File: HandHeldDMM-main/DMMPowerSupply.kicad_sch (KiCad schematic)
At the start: 30 parts, among them J8 Conn_01x01, J9 Conn_01x01, U12 XC62KN33302PR-G, U2 LM358, U8 AMS1117-3.3

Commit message: More pcb work
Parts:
- R24: footprint Resistor_SMD:R_0402_1005Metric_Pad0.72x0.64mm_HandSolder -> Resistor_SMD:R_0603_1608Metric_Pad0.98x0.95mm_HandSolder; LCSC Price 0.05 -> 0.09; Store https://www.lcsc.com/product-detail/Chip-Resistor-Surface-Mount_FOJAN-FRC0402P000-TS_C2906877.html -> https://www.lcsc.com/product-detail/Chip-Resistor-Surface-Mount_FOJAN-FRC0603P000-TS_C2907080.html
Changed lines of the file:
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@@
       (effects (font (size 1.27 1.27)))
     )
-    (property "Footprint" "Resistor_SMD:R_0402_1005Metric_Pad0.72x0.64mm_HandSolder" (at 74.295 60.198 90)
+    (property "Footprint" "Resistor_SMD:R_0603_1608Metric_Pad0.98x0.95mm_HandSolder" (at 74.295 60.198 90)
       (effects (font (size 1.27 1.27)) hide)
     )
-    (property "Datasheet" "https://datasheet.lcsc.com/lcsc/2308241947_FOJAN-FRC0402P000-TS_C2906877.pdf" (at 74.295 58.42 0)
+    (property "Datasheet" "https://datasheet.lcsc.com/lcsc/2308241947_FOJAN-FRC0603P000-TS_C2907080.pdf" (at 74.295 58.42 0)
       (effects (font (size 1.27 1.27)) hide)
     )
-    (property "LCSC Price" "0.05" (at 74.295 58.42 0)
+    (property "LCSC Price" "0.09" (at 74.295 58.42 0)
       (effects (font (size 1.27 1.27)) hide)
     )
@@
       (effects (font (size 1.27 1.27)) hide)
     )
-    (property "Store" "https://www.lcsc.com/product-detail/Chip-Resistor-Surface-Mount_FOJAN-FRC0402P000-TS_C2906877.html" (at 74.295 58.42 0)
+    (property "Store" "https://www.lcsc.com/product-detail/Chip-Resistor-Surface-Mount_FOJAN-FRC0603P000-TS_C2907080.html" (at 74.295 58.42 0)
       (effects (font (size 1.27 1.27)) hide)
     )

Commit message: PCB rev 1 with schematic change ideas
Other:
- note added: "Voltage doubler - Larger input voltage for easier rail splitting - Larger opamp supply voltage helps reduce common mode noise"
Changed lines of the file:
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@@
+    (effects (font (size 1.27 1.27)) (justify left bottom))
+  )
+  (text "Voltage doubler\n- Larger input voltage for easier rail splitting\n- Larger opamp supply voltage helps reduce common mode noise"
+    (at 63.5 -1.27 0)
     (effects (font (size 1.27 1.27)) (justify left bottom))
   )

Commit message: Its going
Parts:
- removed C10 (x4): 1uF, Capacitor_SMD:C_0402_1005Metric_Pad0.74x0.62mm_HandSolder, symbol Device:C
- removed C15, C24: 10uF, Capacitor_SMD:C_0603_1608Metric_Pad1.08x0.95mm_HandSolder, symbol Device:C
- removed C17, C19, C21, C22: 100nF, Capacitor_SMD:C_0402_1005Metric_Pad0.74x0.62mm_HandSolder, symbol Device:C
- removed D1: LED, LED_SMD:LED_0603_1608Metric_Pad1.05x0.95mm_HandSolder, symbol Device:LED
- removed R1, R3: 100K, Resistor_SMD:R_0603_1608Metric_Pad0.98x0.95mm_HandSolder, symbol Device:R
- removed R12: 1k, Resistor_SMD:R_0603_1608Metric_Pad0.98x0.95mm_HandSolder, symbol Device:R
- removed R24: 0R, Resistor_SMD:R_0603_1608Metric_Pad0.98x0.95mm_HandSolder, symbol Device:R
- removed TP1, TP2, TP3, TP4: TestPoint, TestPoint:TestPoint_Pad_D2.0mm, symbol Connector:TestPoint
- removed U12: XC62KN33302PR-G, Package_TO_SOT_SMD:SOT-89-3, symbol Regulator_Linear:XC6206PxxxMR
- removed U2: LM358, Package_SO:SOP-8_3.9x4.9mm_P1.27mm, symbol Amplifier_Operational:LM358
- added C10 (x2): 1uF, Capacitor_SMD:C_0402_1005Metric_Pad0.74x0.62mm_HandSolder, symbol Device:C
- added C28, C36, C37, C39: 10uf, symbol Device:C_Polarized
- added C38, C40: C, symbol Device:C
- added C42, C43: 100nF, Capacitor_SMD:C_0402_1005Metric_Pad0.74x0.62mm_HandSolder, symbol Device:C
- added D4, D5: D, symbol Device:D
- added D6: LED, LED_SMD:LED_0603_1608Metric_Pad1.05x0.95mm_HandSolder, symbol Device:LED
- added R67: 1k, Resistor_SMD:R_0603_1608Metric_Pad0.98x0.95mm_HandSolder, symbol Device:R
- added U24: AMS1117-5.0, Package_TO_SOT_SMD:SOT-223-3_TabPin2, symbol Regulator_Linear:AMS1117-5.0
- added U26, U27, U28: TL7660CDR, Package_SO:SOIC-8_3.9x4.9mm_P1.27mm, symbol Regulator_SwitchedCapacitor:LMC7660
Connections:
- net BattOut- is gone; now on net GND: J9.1 (Pin_1)
- net GND: now also C10.2, C10.2, C37.1, C39.1, C40.1, C42.2, C43.2, R67.2, U24.1 (GND), U26.8 (V+), U27.3 (GND), U28.3 (GND), U28.5 (VOUT)
- net BattOut+ renamed +9V
- net +9V: now also C10.1, C42.1, U24.3 (VI), U27.8 (V+)
- new net: D4.2 (A), U28.8 (V+)
- new net: C28.1, U26.2 (CAP+)
- new net: C37.2, U26.3 (GND), U27.5 (VOUT)
- new net: C28.2, U26.4 (CAP-)
- new net: C36.1, U27.2 (CAP+)
- new net: C36.2, U27.4 (CAP-)
- new net: C38.2, D4.1 (K), D5.2 (A)
- new net: D6.1 (K), R67.1
- new net +5V: C10.1, C43.1, D6.2 (A), U24.2 (VO)
- new net CAP+: C38.1, U28.2 (CAP+)
- new net OpAmpSupply+: C40.2, D5.1 (K)
- new net OpAmpSupply-: C39.2, U26.5 (VOUT)
- no-connect marks 0 -> 7
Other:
- note added: "3v3 reg"
- note added: "5v reg"
- note added: "Is 25 volts possible??? 9 * 2 = 18 * 2 = 36??? Very little needed current No-input voltage for pos is 10 max can get 18V out"
- note added: "LOW ESR!!!"
- note added: "OpAmp +-18V Supply"
- note added: "Smaller test points???"
- note removed: "1/2 batt voltage to -3v3 reg"
- note removed: "1/2 batt voltage to 3v3 reg"
- note removed: "Incase resistor needs added for output stability"
- note removed: "Voltage splitter"
- note removed: "unused opamp"
- moved on the sheet: C10, C4, C5, D2, J8, J9, R9, U8

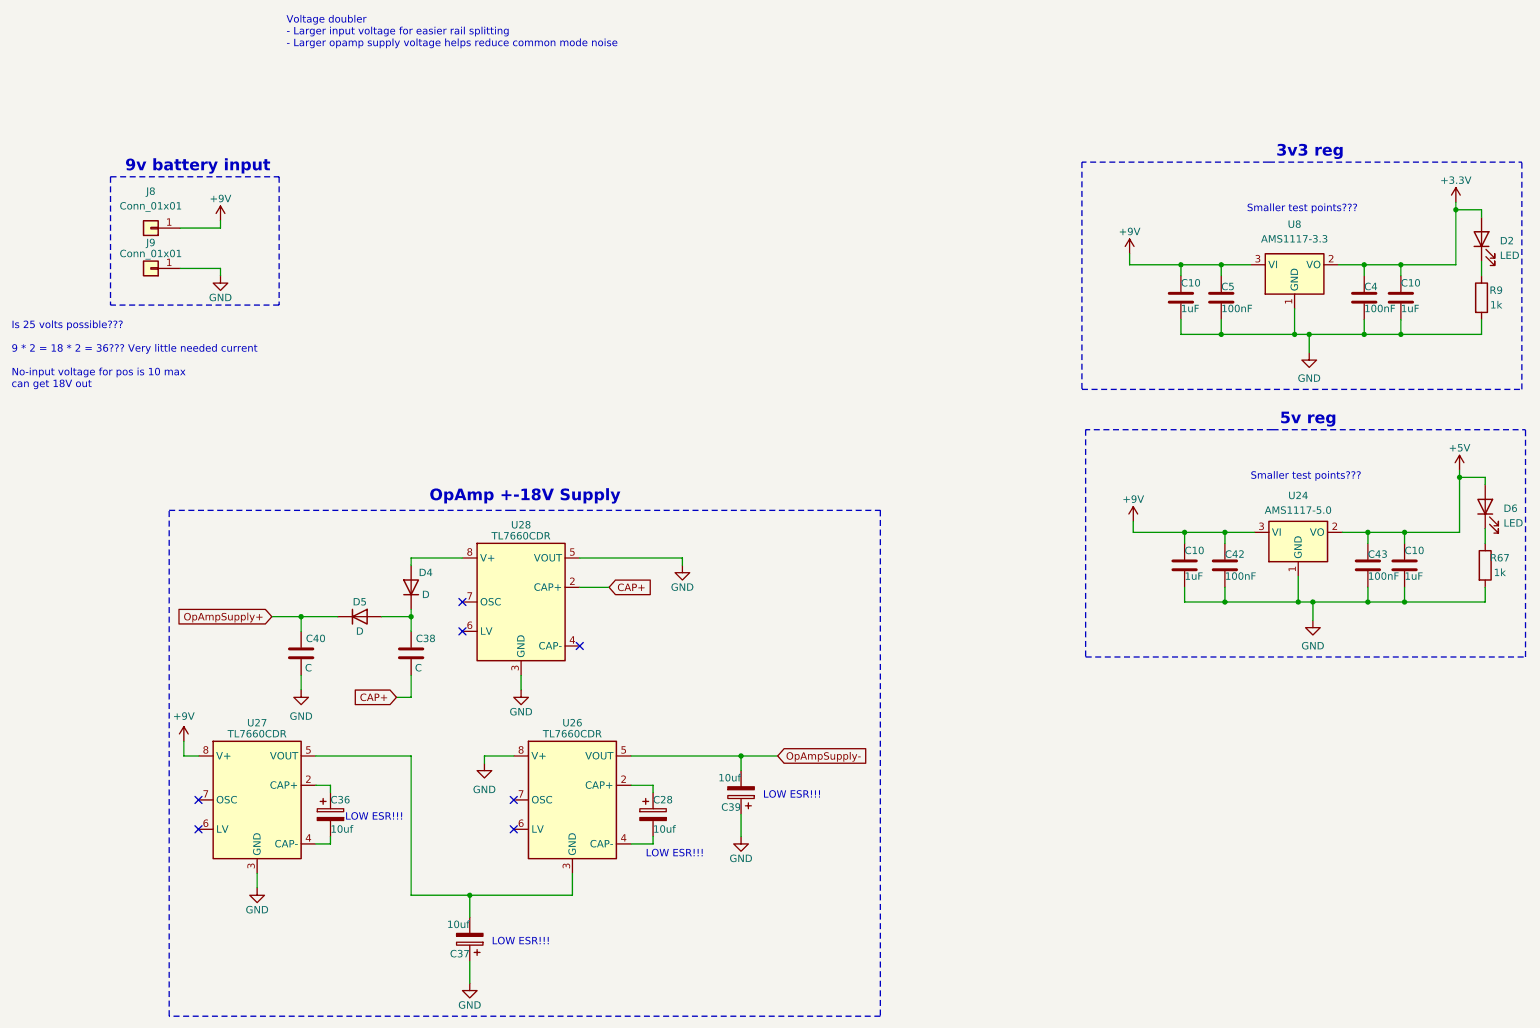
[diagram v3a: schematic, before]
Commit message: Layout / routing V2 with schematic fixes
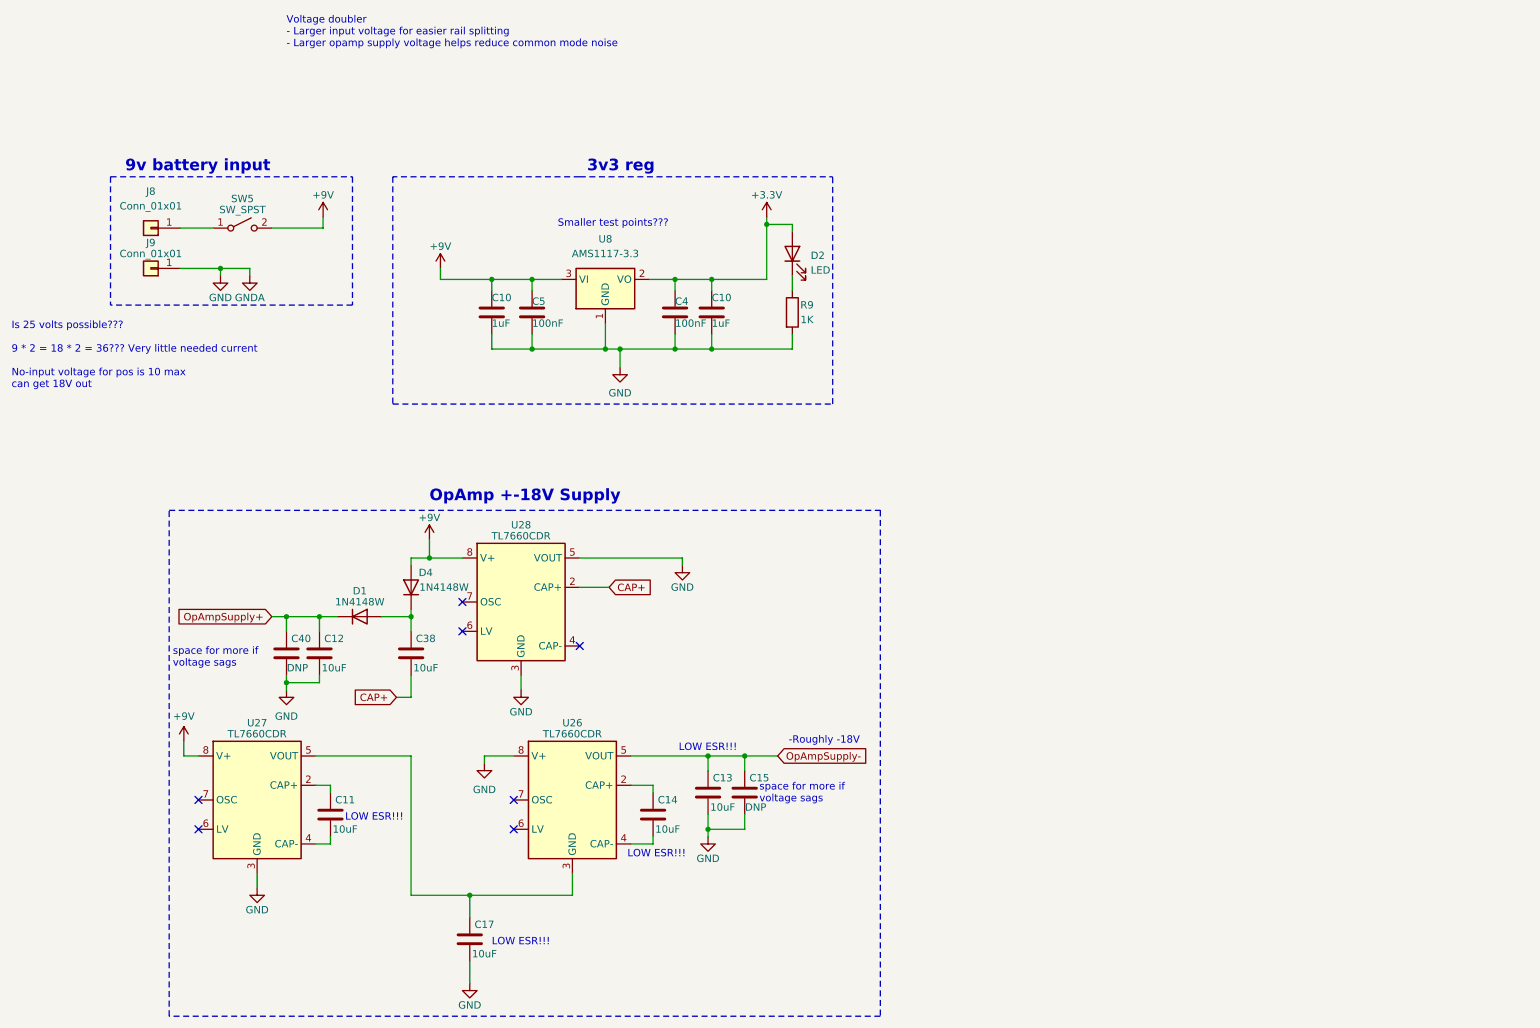
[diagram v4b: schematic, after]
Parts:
- removed C10 (x2): 1uF, Capacitor_SMD:C_0402_1005Metric_Pad0.74x0.62mm_HandSolder, symbol Device:C
- removed C28, C36, C37, C39: 10uf, symbol Device:C_Polarized
- removed C42, C43: 100nF, Capacitor_SMD:C_0402_1005Metric_Pad0.74x0.62mm_HandSolder, symbol Device:C
- removed D5: D, symbol Device:D
- removed D6: LED, LED_SMD:LED_0603_1608Metric_Pad1.05x0.95mm_HandSolder, symbol Device:LED
- removed R67: 1k, Resistor_SMD:R_0603_1608Metric_Pad0.98x0.95mm_HandSolder, symbol Device:R
- removed U24: AMS1117-5.0, Package_TO_SOT_SMD:SOT-223-3_TabPin2, symbol Regulator_Linear:AMS1117-5.0
- added C11, C12, C13, C14, C17: 10uF, Capacitor_SMD:C_1206_3216Metric_Pad1.33x1.80mm_HandSolder, symbol Device:C
- added C15: DNP, Capacitor_SMD:C_1206_3216Metric_Pad1.33x1.80mm_HandSolder, symbol Device:C
- added D1: 1N4148W, Diode_SMD:D_SOD-123, symbol Device:D
- added SW5: SW_SPST, Custom Lib:Dip Switch, symbol Switch:SW_SPST
- C10: PART# (none) -> C14445; Price / 1 (none) -> 0.0017
- C38: value C -> 10uF; footprint (none) -> Capacitor_SMD:C_1206_3216Metric_Pad1.33x1.80mm_HandSolder; LCSC Price (none) -> 0.41; PART# (none) -> C5189826; Price / 1 (none) -> 0.0206; Price Qty (none) -> 20; Store (none) -> https://www.lcsc.com/product-detail/Multilayer-Ceramic-Capa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
- C4, C5: LCSC Price 0 -> 0.18; PART# (none) -> C513772; Price / 1 (none) -> 0.0018; Price Qty 0 -> 100; Store Parts Bin -> https://www.lcsc.com/product-detail/Multilayer-Ceramic-Capa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
- C40: value C -> DNP; footprint (none) -> Capacitor_SMD:C_1206_3216Metric_Pad1.33x1.80mm_HandSolder
- D4: value D -> 1N4148W; footprint (none) -> Diode_SMD:D_SOD-123; LCSC Price (none) -> 0.52; PART# (none) -> 1N4148W; Price / 1 (none) -> 0.0052; Price Qty (none) -> 100; Store (none) -> https://www.lcsc.com/product-detail/Switching-span-style-ba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
- R9: value 1k -> 1K; PART# (none) -> C5141145; Price / 1 (none) -> 0.0049
- U26, U27, U28: LCSC https://www.lcsc.com/product-detail/DC-DC-Converters_Texas-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 -> (none); Store (none) -> https://www.lcsc.com/product-detail/DC-DC-Converters_Texas-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
- U8: PART# (none) -> C5345982; Price / 1 (none) -> 0.0392
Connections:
- net +9V: now also D4.2 (A), U28.8 (V+), SW5.2 (B); no longer J8.1 (Pin_1)
- net GND: now also C12.1, C13.1, C15.1, C17.1
- net OpAmpSupply+: now also C12.2, D1.1 (K)
- net OpAmpSupply-: now also C13.2, C15.2
- net at U26.2 (CAP+): now also C14.2
- net at U26.3 (GND), U27.5 (VOUT): now also C17.2
- net at U26.4 (CAP-): now also C14.1
- net at U27.2 (CAP+): now also C11.2
- net at U27.4 (CAP-): now also C11.1
- net at C38.2, D4.1 (K): now also D1.2 (A)
- new net: J8.1 (Pin_1), SW5.1 (A)
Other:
- note added: "-Roughly -18V"
- note added: "space for more if voltage sags"
- note removed: "5v reg"
- moved on the sheet: C10, C4, C40, C5, D2, R9, U8

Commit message: Ordered
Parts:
- D1, D4: PART# 1N4148W -> C917030
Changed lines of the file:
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@@
       (effects (font (size 1.27 1.27)) hide)
     )
-    (property "PART#" "1N4148W" (at 85.09 92.075 0)
+    (property "PART#" "C917030" (at 85.09 92.075 0)
       (effects (font (size 1.27 1.27)) hide)
     )
@@
       (effects (font (size 1.27 1.27)) hide)
     )
-    (property "PART#" "1N4148W" (at 76.2 97.155 0)
+    (property "PART#" "C917030" (at 76.2 97.155 0)
       (effects (font (size 1.27 1.27)) hide)
     )

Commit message: fixes for v2
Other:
- note added: "LV to GND"
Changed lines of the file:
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@@
     (effects (font (size 2 2) (thickness 0.4) bold) (justify left bottom))
+  )
+  (text "LV to GND\n" (at 68.58 154.94 0)
+    (effects (font (size 1.27 1.27)) (justify left bottom))
   )
   (text "Smaller test points???" (at 110.49 29.845 0)
